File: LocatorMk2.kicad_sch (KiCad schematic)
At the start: 41 parts

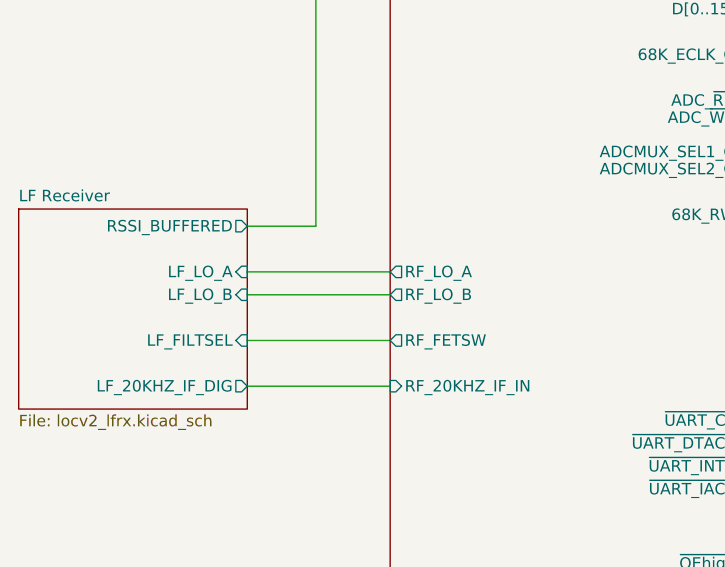
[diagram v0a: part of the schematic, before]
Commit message: Rev B: Fix: Fixed/Variable LO swapped at SA605
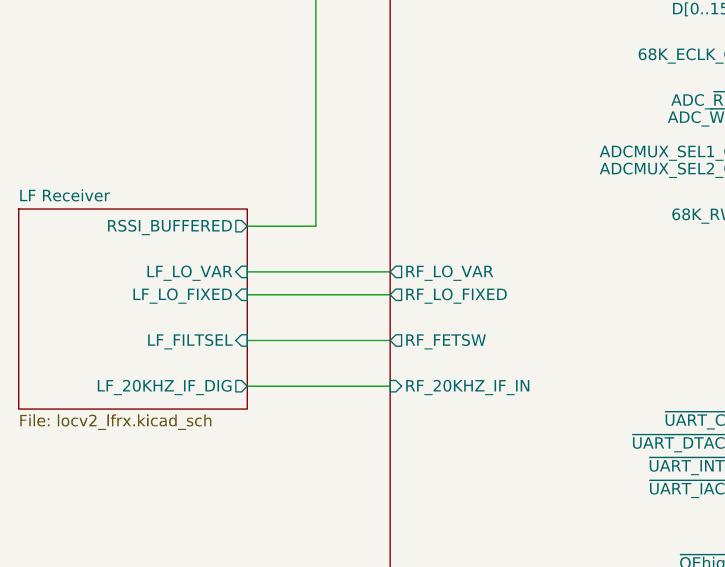
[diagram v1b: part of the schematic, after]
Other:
- sheet 68000 CPU and ASIC ports: added RF_LO_FIXED, RF_LO_VAR; removed RF_LO_A, RF_LO_B
- sheet LF Receiver ports: added LF_LO_FIXED, LF_LO_VAR; removed LF_LO_A, LF_LO_B
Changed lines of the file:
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@@
   (title_block
     (title "Datatrak Locator Mk.2")
-    (date "2022-06-29")
-    (rev "A")
+    (date "2022-07-08")
+    (rev "B")
   )
   (junction (at 154.305 241.935) (diameter 0) (color 0 0 0 0)
@@
       (effects (font (size 1.27 1.27)) (justify right))
     )
-    (pin "RF_LO_A" output (at 60.96 73.66 180)
+    (pin "RF_LO_VAR" output (at 60.96 73.66 180)
       (effects (font (size 1.27 1.27)) (justify left))
     )
@@
       (effects (font (size 1.27 1.27)) (justify left))
     )
-    (pin "RF_LO_B" output (at 60.96 76.2 180)
+    (pin "RF_LO_FIXED" output (at 60.96 76.2 180)
       (effects (font (size 1.27 1.27)) (justify left))
     )
@@
       (effects (font (size 1.27 1.27)) (justify left top))
     )
-    (pin "LF_LO_A" input (at 45.085 73.66 0)
-      (effects (font (size 1.27 1.27)) (justify right))
-    )
-    (pin "LF_LO_B" input (at 45.085 76.2 0)
-      (effects (font (size 1.27 1.27)) (justify right))
-    )
+    (pin "LF_LO_VAR" input (at 45.085 73.66 0)
+      (effects (font (size 1.27 1.27)) (justify right))
+    )
+    (pin "LF_LO_FIXED" input (at 45.085 76.2 0)
+      (effects (font (size 1.27 1.27)) (justify right))
+    )
